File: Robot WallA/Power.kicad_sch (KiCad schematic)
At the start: 15 parts, among them IC5 TLV75533PDBVR, J1 XT90PW_M, J10 Conn_01x02_Pin, J15 Conn_01x02, J17 Conn_01x02, J9 Conn_01x02

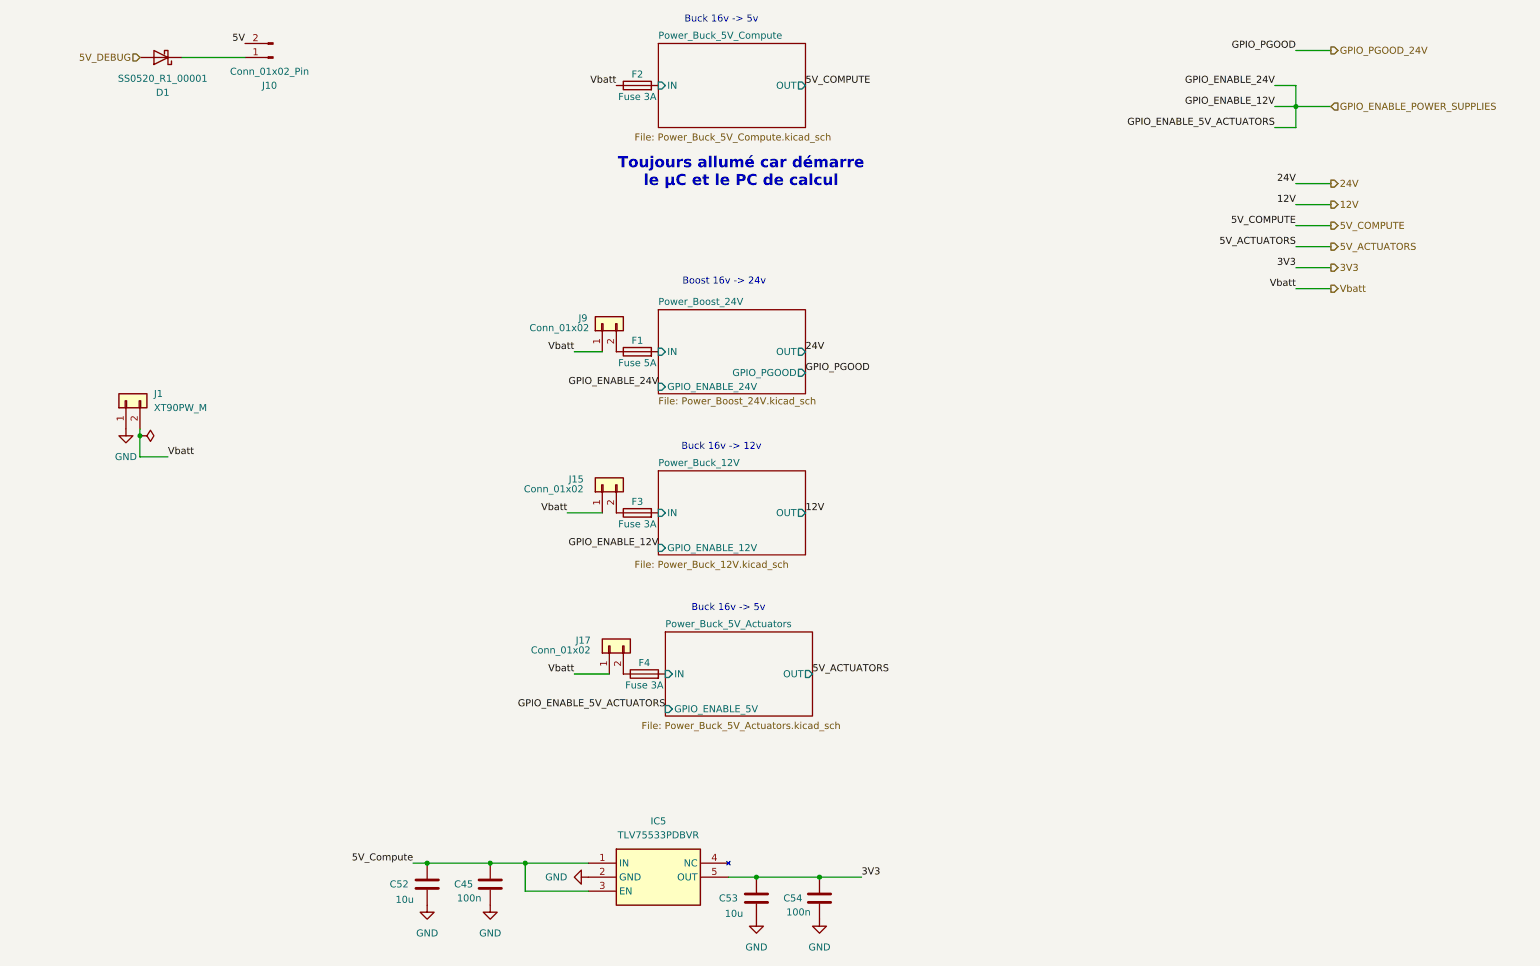
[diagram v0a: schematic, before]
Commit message: Continued to link MCU pins, Added a sheet for servomotors and optional 2 DC motors.
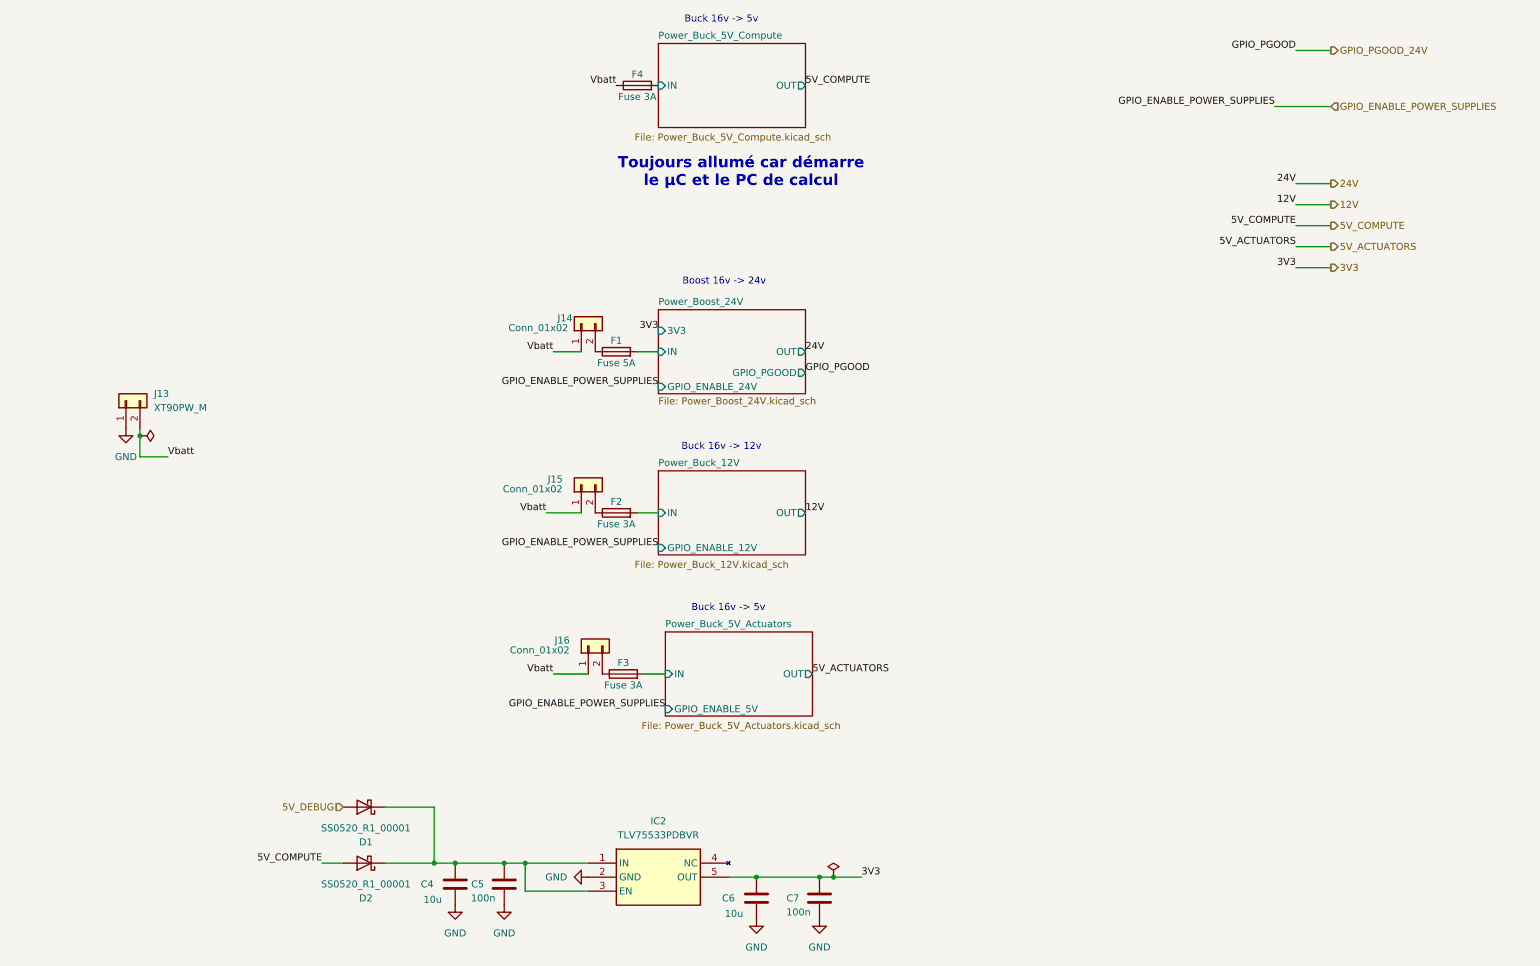
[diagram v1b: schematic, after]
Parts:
- removed J10: Conn_01x02_Pin, symbol Connector:Conn_01x02_Pin
- added D2: SS0520_R1_00001, symbol Device:D_Schottky
- renumbered C52 to C4, C45 to C5, C53 to C6, C54 to C7, F3 to F2, F4 to F3, F2 to F4, IC5 to IC2, J1 to J13, J9 to J14, J17 to J16
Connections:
- net 5V_Compute is gone; now on an unnamed net: C4.1, C5.1, IC2.1 (IN), IC2.3 (EN)
- net 5V_COMPUTE: now also D2.2 (A)
- net at D1.1 (K): now also D2.1 (K)
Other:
- sheet Power_Boost_24V ports: added 3V3; removed none
- moved on the sheet: C4, C5, D1, F1, F2, F3, J14, J15, J16

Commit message: Defined every footprints
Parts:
- C36: renamed from C4; value 10u -> 10uF; footprint (none) -> Capacitor_SMD:C_0603_1608Metric_Pad1.08x0.95mm_HandSolder
- C37: renamed from C5; value 100n -> 100nF; footprint (none) -> Capacitor_SMD:C_0603_1608Metric_Pad1.08x0.95mm_HandSolder
- C38: renamed from C6; value 10u -> 10uF; footprint (none) -> Capacitor_SMD:C_0603_1608Metric_Pad1.08x0.95mm_HandSolder
- C39: renamed from C7; value 100n -> 100nF; footprint (none) -> Capacitor_SMD:C_0603_1608Metric_Pad1.08x0.95mm_HandSolder
- D3: renamed from D1; footprint (none) -> Diode_SMD:D_SOD-123; Manufacturer_Part_Number (none) -> SS0520_R1_00001
- D4: renamed from D2; footprint (none) -> Diode_SMD:D_SOD-123; Manufacturer_Part_Number (none) -> SS0520_R1_00001
- F1: renamed from F4; footprint (none) -> Fuse:Fuse_1206_3216Metric; Manufacturer_Part_Number (none) -> JB12F3001R
- F2: renamed from F1; footprint (none) -> Fuse:Fuse_1206_3216Metric; Manufacturer_Part_Number (none) -> JB12S5001R
- F3: renamed from F2; footprint (none) -> Fuse:Fuse_1206_3216Metric; Manufacturer_Part_Number (none) -> JB12F3001R
- F4: renamed from F3; footprint (none) -> Fuse:Fuse_1206_3216Metric; Manufacturer_Part_Number (none) -> JB12F3001R
- IC6: renamed from IC2; footprint SOT95P280X145-5N -> SamacSys_Parts:SOT95P280X145-5N; Arrow Part Number TLV75533PDBVR -> (none); Arrow Price/Stock https://www.arrow.com/en/products/tlv75533pdbvr/texas-instr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 -> (none); Height 1.45 -> (none); Manufacturer_Name Texas Instruments -> (none); Mouser Part Number 595-TLV75533PDBVR -> (none); Mouser Price/Stock https://www.mouser.co.uk/ProductDetail/Texas-Instruments/TL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 -> (none)
- renumbered J16 to J10, J14 to J7, J13 to J8, J15 to J9

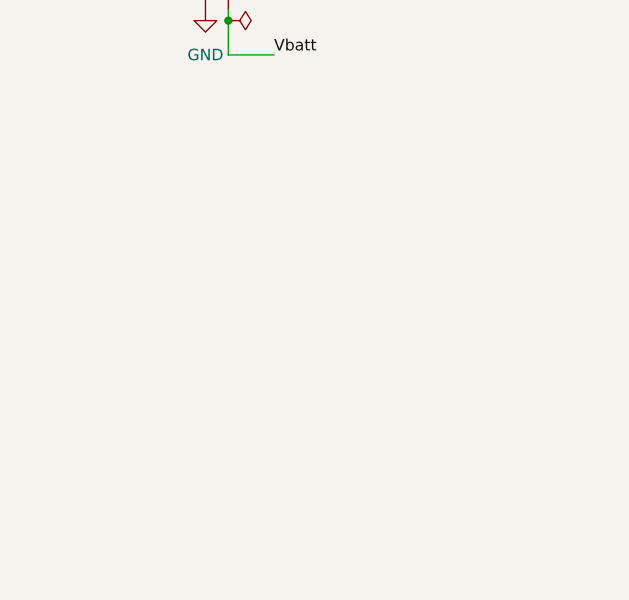
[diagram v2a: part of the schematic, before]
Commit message: Updated README and add jumper part reference
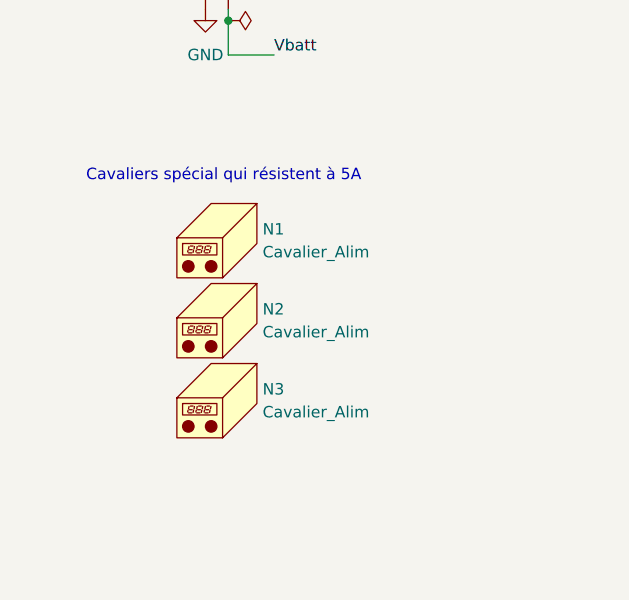
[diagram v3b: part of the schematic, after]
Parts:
- added N1, N2, N3: Cavalier_Alim, symbol Mechanical:Housing
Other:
- note added: "Cavaliers spécial qui résistent à 5A"
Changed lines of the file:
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@@
 	(generator_version "9.0")
 	(paper "A4")
+	(text "Cavaliers spécial qui résistent à 5A"
+		(exclude_from_sim no)
+		(at 36.322 112.522 0)
+		(effects
+			(font
+				(size 1.27 1.27)
+			)
+		)
+	)
 	(text "Buck 16v -> 12v"
 		(exclude_from_sim no)
@@
 	)
 	(symbol
+		(lib_id "Mechanical:Housing")
+		(at 36.83 137.16 0)
+		(unit 1)
+		(exclude_from_sim no)
+		(in_bom yes)
+		(on_board no)
+		(dnp no)
+		(property "Reference" "N3"
+			(at 40.64 136.2074 0)
+			(effects
+				(font
+					(size 1.27 1.27)
+				)
+				(justify left)
+			)
+		)
+		(property "Value" "Cavalier_Alim"
+			(at 40.64 138.7474 0)
+			(effects
+				(font
+					(size 1.27 1.27)
+				)
+				(justify left)
+			)
+		)
+		(property "Footprint" ""
+			(at 38.1 135.89 0)
+			(effects
+				(font
+					(size 1.27 1.27)
+				)
+				(hide yes)
+			)
+		)
+		(property "Datasheet" "~"
+			(at 38.1 135.89 0)
+			(effects
+				(font
+					(size 1.27 1.27)
+				)
+				(hide yes)
+			)
+		)
+		(property "Description" "Housing"
+			(at 36.83 137.16 0)
+			(effects
+				(font
+					(size 1.27 1.27)
+				)
+				(hide yes)
+			)
+		)
+		(property "Manufacturer_Part_Number" "15-29-1024"
+			(at 36.83 137.16 0)
+			(effects
+				(font
+					(size 1.27 1.27)
+				)
+				(hide yes)
+			)
+		)
+		(instances
+			(project "Robot WallA"
+				(path "/117fd49e-499d-4b54-b58c-f6b538ecca4a/d5f4dab0-e2de-4083-971d-4b1eb9c8d4bb"
+					(reference "N3")
+					(unit 1)
+				)
+			)
+		)
+	)
+	(symbol
 		(lib_id "power:GND")
 		(at 148.59 182.88 0)
@@
 	)
 	(symbol
+		(lib_id "Mechanical:Housing")
+		(at 36.83 128.27 0)
+		(unit 1)
+		(exclude_from_sim no)
+		(in_bom yes)
+		(on_board no)
+		(dnp no)
+		(property "Reference" "N2"
+			(at 40.64 127.3174 0)
+			(effects
+				(font
+					(size 1.27 1.27)
+				)
+				(justify left)
+			)
+		)
+		(property "Value" "Cavalier_Alim"
+			(at 40.64 129.8574 0)
+			(effects
+				(font
+					(size 1.27 1.27)
+				)
+				(justify left)
+			)
+		)
+		(property "Footprint" ""
+			(at 38.1 127 0)
+			(effects
+				(font
+					(size 1.27 1.27)
+				)
+				(hide yes)
+			)
+		)
+		(property "Datasheet" "~"
+			(at 38.1 127 0)
+			(effects
+				(font
+					(size 1.27 1.27)
+				)
+				(hide yes)
+			)
+		)
+		(property "Description" "Housing"
+			(at 36.83 128.27 0)
+			(effects
+				(font
+					(size 1.27 1.27)
+				)
+				(hide yes)
+			)
+		)
+		(property "Manufacturer_Part_Number" "15-29-1024"
+			(at 36.83 128.27 0)
+			(effects
+				(font
+					(size 1.27 1.27)
+				)
+				(hide yes)
+			)
+		)
+		(instances
+			(project "Robot WallA"
+				(path "/117fd49e-499d-4b54-b58c-f6b538ecca4a/d5f4dab0-e2de-4083-971d-4b1eb9c8d4bb"
+					(reference "N2")
+					(unit 1)
+				)
+			)
+		)
+	)
+	(symbol
 		(lib_id "Device:Fuse")
 		(at 127 31.75 90)
@@
 					(unit 1)
 				)
+			)
+		)
+	)
+	(symbol
+		(lib_id "Mechanical:Housing")
+		(at 36.83 119.38 0)
+		(unit 1)
+		(exclude_from_sim no)
+		(in_bom yes)
+		(on_board no)
+		(dnp no)
+		(property "Reference" "N1"
+			(at 40.64 118.4274 0)
+			(effects
+				(font
+					(size 1.27 1.27)
+				)
+				(justify left)
+			)
+		)
+		(property "Value" "Cavalier_Alim"
+			(at 40.64 120.9674 0)
+			(effects
+				(font
+					(size 1.27 1.27)
+				)
+				(justify left)
+			)
+		)
+		(property "Footprint" ""
+			(at 38.1 118.11 0)
+			(effects
+				(font
+					(size 1.27 1.27)
+				)
+				(hide yes)
+			)
+		)
+		(property "Datasheet" "~"
+			(at 38.1 118.11 0)
+			(effects
+				(font
+					(size 1.27 1.27)
+				)
+				(hide yes)
+			)
+		)
+		(property "Description" "Housing"
+			(at 36.83 119.38 0)
+			(effects
+				(font
+					(size 1.27 1.27)
+				)
+				(hide yes)
+			)
+		)
+		(property "Manufacturer_Part_Number" "15-29-1024"
+			(at 36.83 119.38 0)
+			(effects
+				(font
+					(size 1.27 1.27)
+				)
+				(hide yes)
+			)
+		)
+		(instances
+			(project ""
+				(path "/117fd49e-499d-4b54-b58c-f6b538ecca4a/d5f4dab0-e2de-4083-971d-4b1eb9c8d4bb"
+					(reference "N1")
+					(unit 1)
+				)

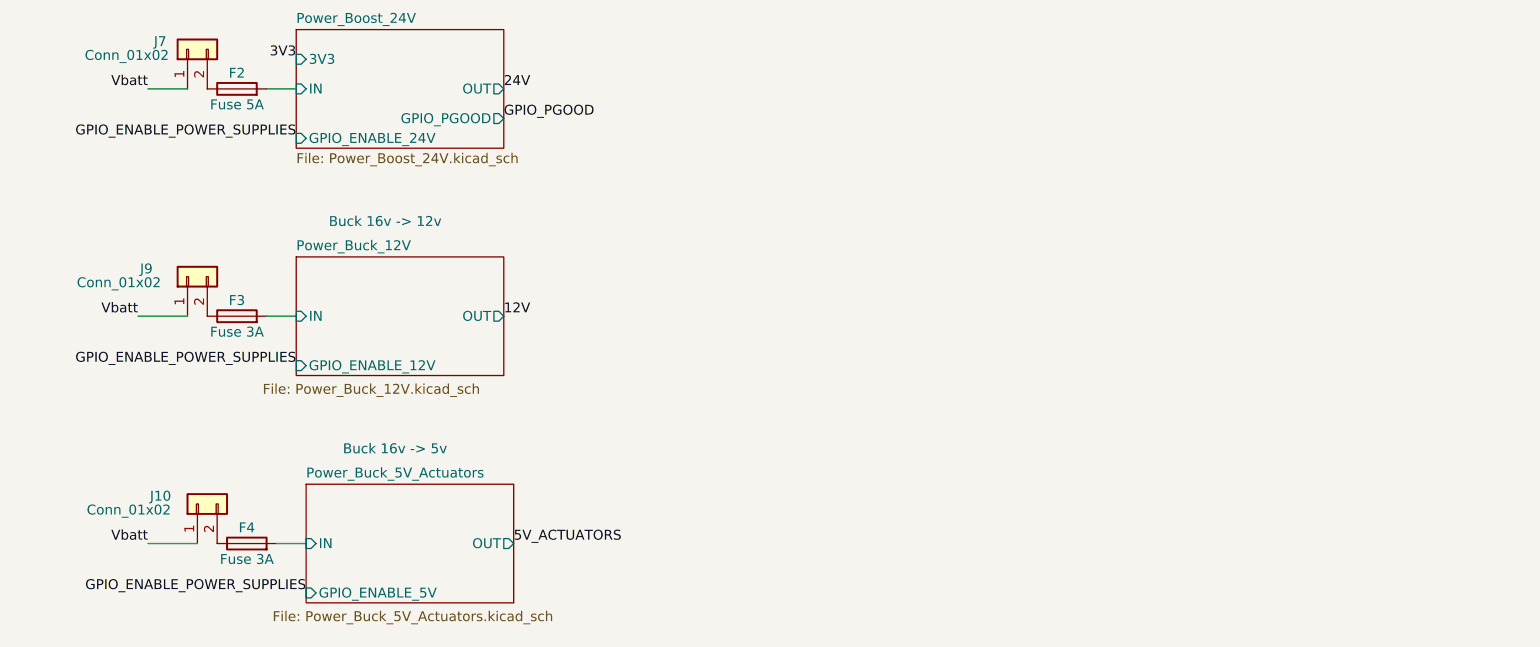
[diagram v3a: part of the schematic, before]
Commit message: Updated USB UART converter, Linked telemeter sensors.
Updated components indicators
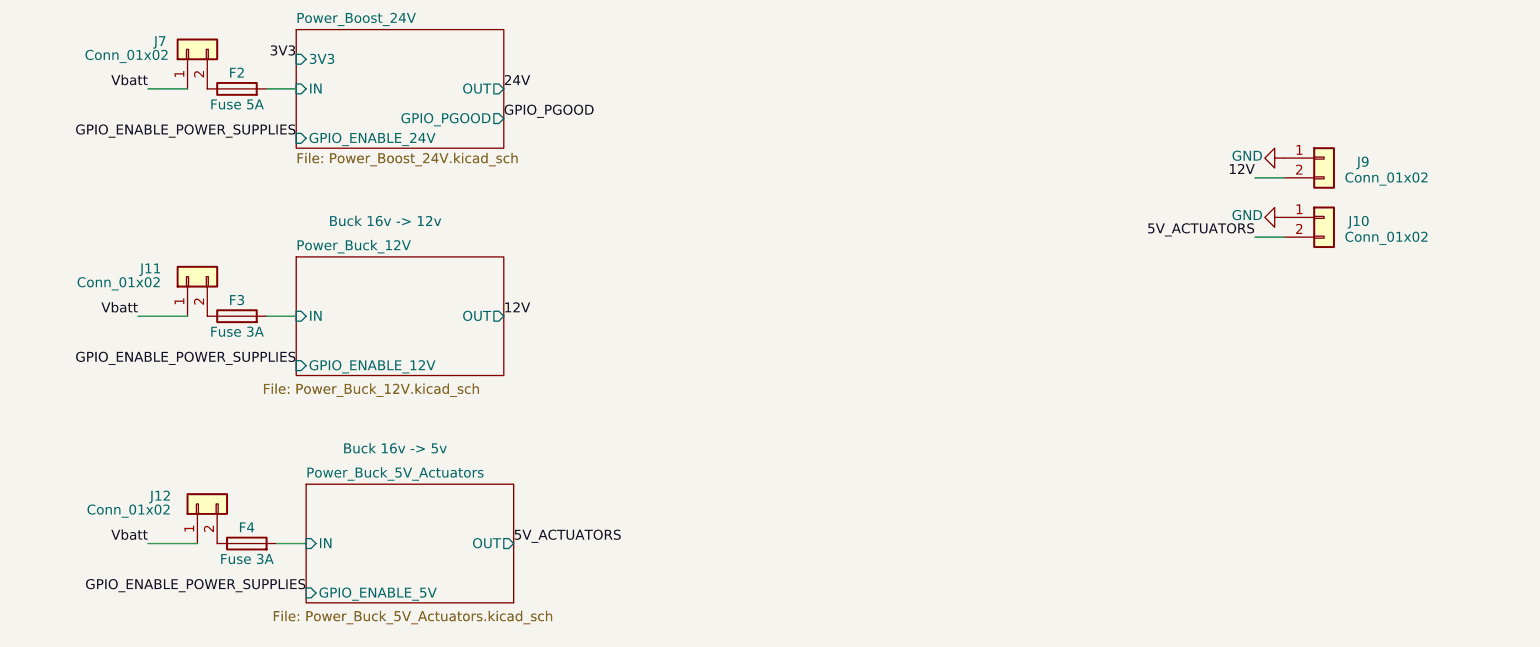
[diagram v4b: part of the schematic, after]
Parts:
- added J10, J9: Conn_01x02, SamacSys_Parts:SHDR2W50P0X200_1X2_590X450X600P, symbol Connector_Generic:Conn_01x02
- renumbered J9 to J11, J10 to J12
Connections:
- net 12V: now also J9.2 (Pin_2)
- net 5V_ACTUATORS: now also J10.2 (Pin_2)
- net GND: now also J10.1 (Pin_1), J9.1 (Pin_1)

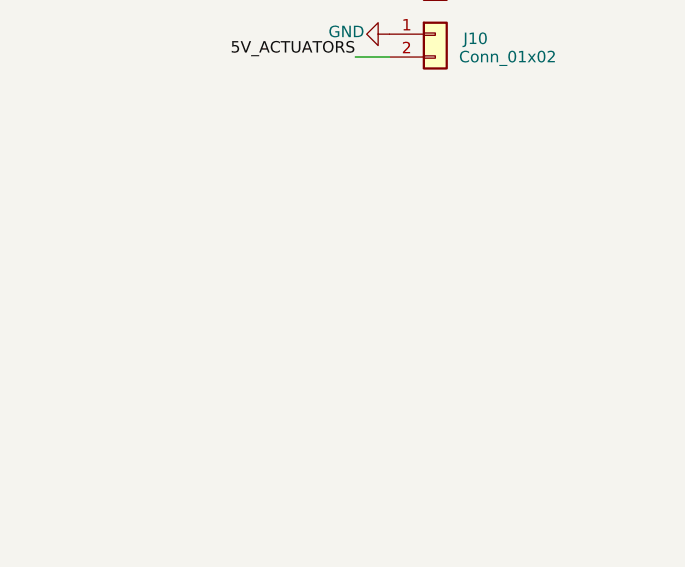
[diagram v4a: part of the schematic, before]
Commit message: Added standard switchs, debug leds and 12V and 5V connectors
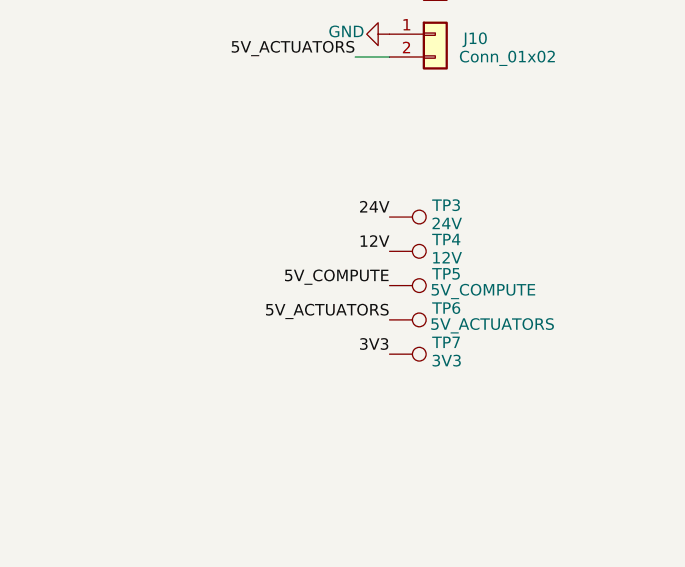
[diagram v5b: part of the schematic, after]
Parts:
- added TP3: 24V, TestPoint:TestPoint_Pad_D2.0mm, symbol Connector:TestPoint
- added TP4: 12V, TestPoint:TestPoint_Pad_D2.0mm, symbol Connector:TestPoint
- added TP5: 5V_COMPUTE, TestPoint:TestPoint_Pad_D2.0mm, symbol Connector:TestPoint
- added TP6: 5V_ACTUATORS, TestPoint:TestPoint_Pad_D2.0mm, symbol Connector:TestPoint
- added TP7: 3V3, TestPoint:TestPoint_Pad_D2.0mm, symbol Connector:TestPoint
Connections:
- net 12V: now also TP4.1
- net 24V: now also TP3.1
- net 3V3: now also TP7.1
- net 5V_ACTUATORS: now also TP6.1
- net 5V_COMPUTE: now also TP5.1
